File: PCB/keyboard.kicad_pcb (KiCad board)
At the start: 2 copper layers, 323.9 x 131 mm, 173 parts, among them J1 Conn_01x06_Pin, J2 Conn_01x02_Pin, SW1 SW_Push, SW10 SW_Push, SW11 SW_Push, SW12 SW_Push, SW13 SW_Push, SW14 SW_Push, SW15 RotaryEncoder_Switch, SW16 SW_Push, SW17 SW_Push, SW18 SW_Push, SW19 SW_Push, SW2 SW_Push, SW20 SW_Push, SW21 SW_Push, SW22 SW_Push, SW23 SW_Push, SW24 SW_Push, SW25 SW_Push, SW26 SW_Push, SW27 SW_Push, SW28 SW_Push, SW29 SW_Push, SW3 SW_Push, SW30 SW_Push, SW31 SW_Push, SW32 SW_Push, SW33 SW_Push, SW34 SW_Push, SW35 SW_Push, SW36 SW_Push, SW37 SW_Push, SW38 SW_Push, SW39 SW_Push, SW4 SW_Push, SW40 SW_Push, SW41 SW_Push, SW42 SW_Push, SW43 SW_Push, SW44 SW_Push, SW45 SW_Push, SW46 SW_Push, SW47 SW_Push, SW48 SW_Push, SW49 SW_Push, SW5 SW_Push, SW50 SW_Push, SW51 SW_Push, SW52 SW_Push, SW53 SW_Push, SW54 SW_Push, SW55 SW_Push, SW56 SW_Push, SW57 SW_Push, SW58 SW_Push, SW59 SW_Push, SW6 SW_Push, SW60 SW_Push, SW61 SW_Push, SW62 SW_Push, SW63 SW_Push, SW64 SW_Push, SW65 SW_Push, SW66 SW_Push, SW67 SW_Push, SW68 SW_Push, SW69 SW_Push, SW7 SW_Push, SW70 SW_Push, SW71 SW_Push, SW72 SW_Push, SW73 SW_Push, SW74 SW_Push, SW75 SW_Push, SW76 SW_Push, SW77 SW_Push, SW78 SW_Push, SW79 SW_Push, SW8 SW_Push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

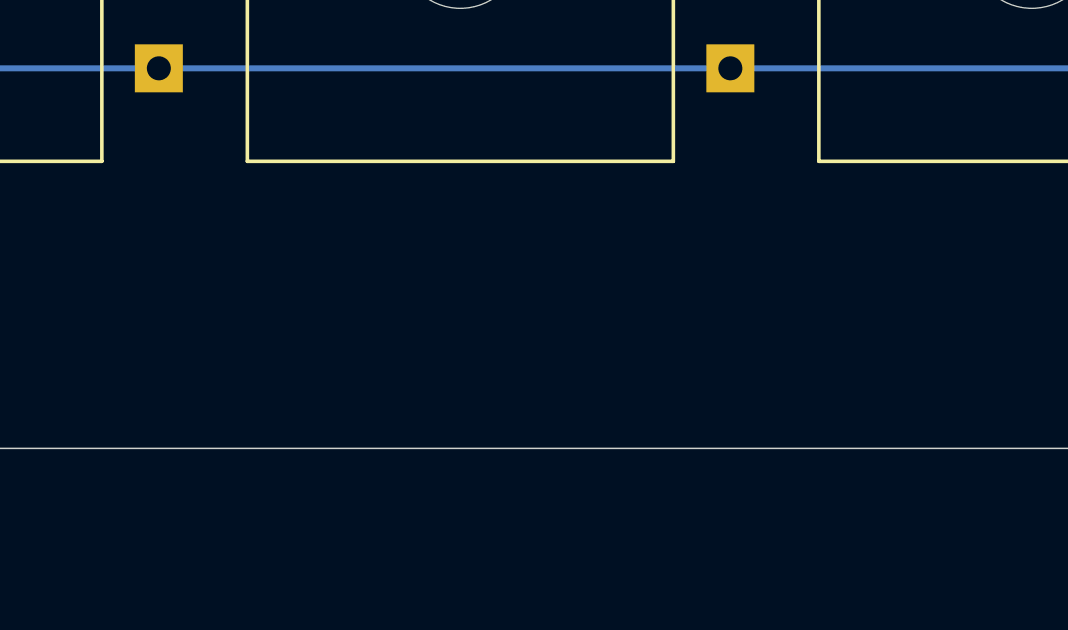
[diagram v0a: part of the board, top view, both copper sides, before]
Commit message: feat: update keyboard pcb and production files
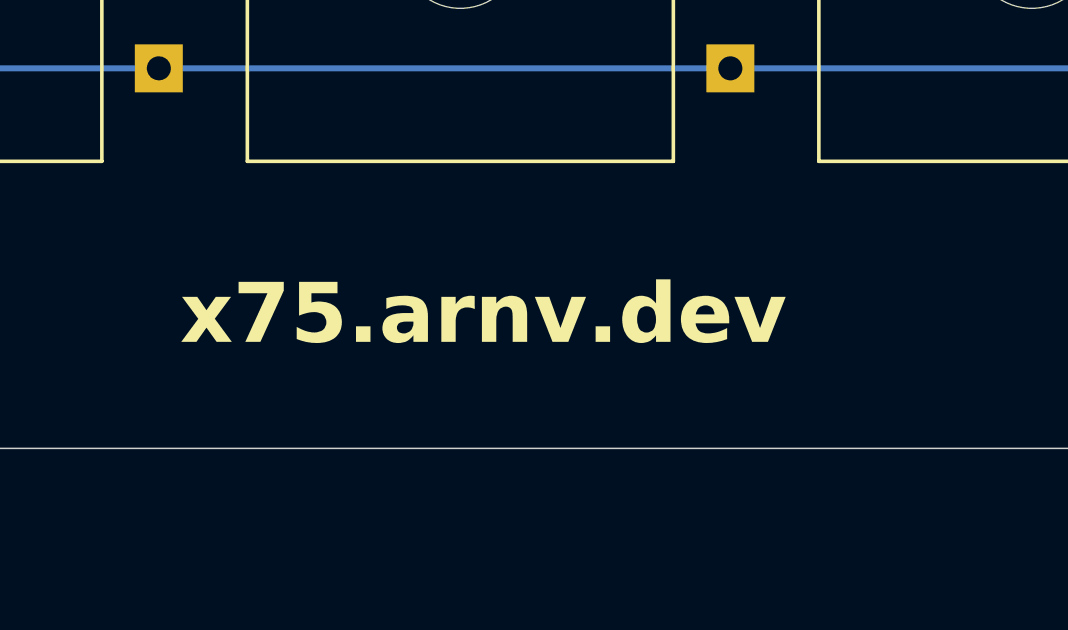
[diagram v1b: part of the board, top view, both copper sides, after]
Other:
- board text added: "x75.arnv.dev"
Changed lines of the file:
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@@
 			(psa4output no)
 			(plot_black_and_white no)
-			(plotinvisibletext no)
 			(sketchpadsonfab no)
 			(plotpadnumbers no)
@@
 		)
 	)
+	(gr_text "x75.arnv.dev"
+		(at 269.89625 198.463396 0)
+		(layer "F.SilkS")
+		(effects
+			(font
+				(size 2 2)
+				(thickness 0.4)
+				(bold yes)
+			)
+			(justify left bottom)
+		)
+	)

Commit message: update gerbers
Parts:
- SW1, SW10, SW11, SW12, SW13, SW14, SW16, SW17, SW18, SW19, SW2, SW20, SW21, SW22, SW23, SW24, SW25, SW26, SW27, SW28, SW3, SW30, SW32, SW33, SW34, SW35, SW36, SW37, SW38, SW39, SW4, SW40, SW41, SW42, SW43, SW45, SW47, SW48, SW49, SW5, SW50, SW51, SW52, SW53, SW54, SW55, SW56, SW57, SW59, SW6, SW61, SW62, SW63, SW64, SW65, SW66, SW67, SW68, SW69, SW7, SW70, SW72, SW73, SW78, SW79, SW8, SW80, SW81, SW82, SW83, SW9: footprint Switch_Keyboard_Hotswap_Kailh:SW_Hotswap_Kailh_MX_Plated_1.00u_With_Switch -> Switch_MX_Hotswap:SW_Hotswap_Kailh_MX_Plated_1.00u_With_Switch
- SW29: footprint Switch_Keyboard_Hotswap_Kailh:SW_Hotswap_Kailh_MX_Plated_2.00u_With_Switch -> Switch_MX_Hotswap:SW_Hotswap_Kailh_MX_Plated_2.00u_With_Switch
- SW31, SW44: footprint Switch_Keyboard_Hotswap_Kailh:SW_Hotswap_Kailh_MX_Plated_1.50u_With_Switch -> Switch_MX_Hotswap:SW_Hotswap_Kailh_MX_Plated_1.50u_With_Switch
- SW46, SW71: footprint Switch_Keyboard_Hotswap_Kailh:SW_Hotswap_Kailh_MX_Plated_1.75u_With_Switch -> Switch_MX_Hotswap:SW_Hotswap_Kailh_MX_Plated_1.75u_With_Switch
- SW58, SW60: footprint Switch_Keyboard_Hotswap_Kailh:SW_Hotswap_Kailh_MX_Plated_2.25u_With_Switch -> Switch_MX_Hotswap:SW_Hotswap_Kailh_MX_Plated_2.25u_With_Switch
- SW74, SW75, SW76: footprint Switch_Keyboard_Hotswap_Kailh:SW_Hotswap_Kailh_MX_Plated_1.25u_With_Switch -> Switch_MX_Hotswap:SW_Hotswap_Kailh_MX_Plated_1.25u_With_Switch
- SW77: footprint Switch_Keyboard_Hotswap_Kailh:SW_Hotswap_Kailh_MX_Plated_6.25u_With_Switch -> Switch_MX_Hotswap:SW_Hotswap_Kailh_MX_Plated_6.25u_With_Switch
